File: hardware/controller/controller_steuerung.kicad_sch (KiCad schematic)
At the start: 79 parts, among them J10 FAN, J3 DISPLAY, J4 PANEL, J5 TC top, J6 TC bot, J7 USB-C, J9 UART, Q6 AO3401A, Q7 IRLML6346, Q8 BSS138, SW1 RESET, SW2 BOOT, U10 USBLC6-2SC6, U11 USBLC6-2SC6, U12 USBLC6-2SC6, U3 ESP32-S3-WROOM-1U-N8, U4 USBLC6-2SC6, U5 MAX31856MUD+, U6 MAX31856MUD+

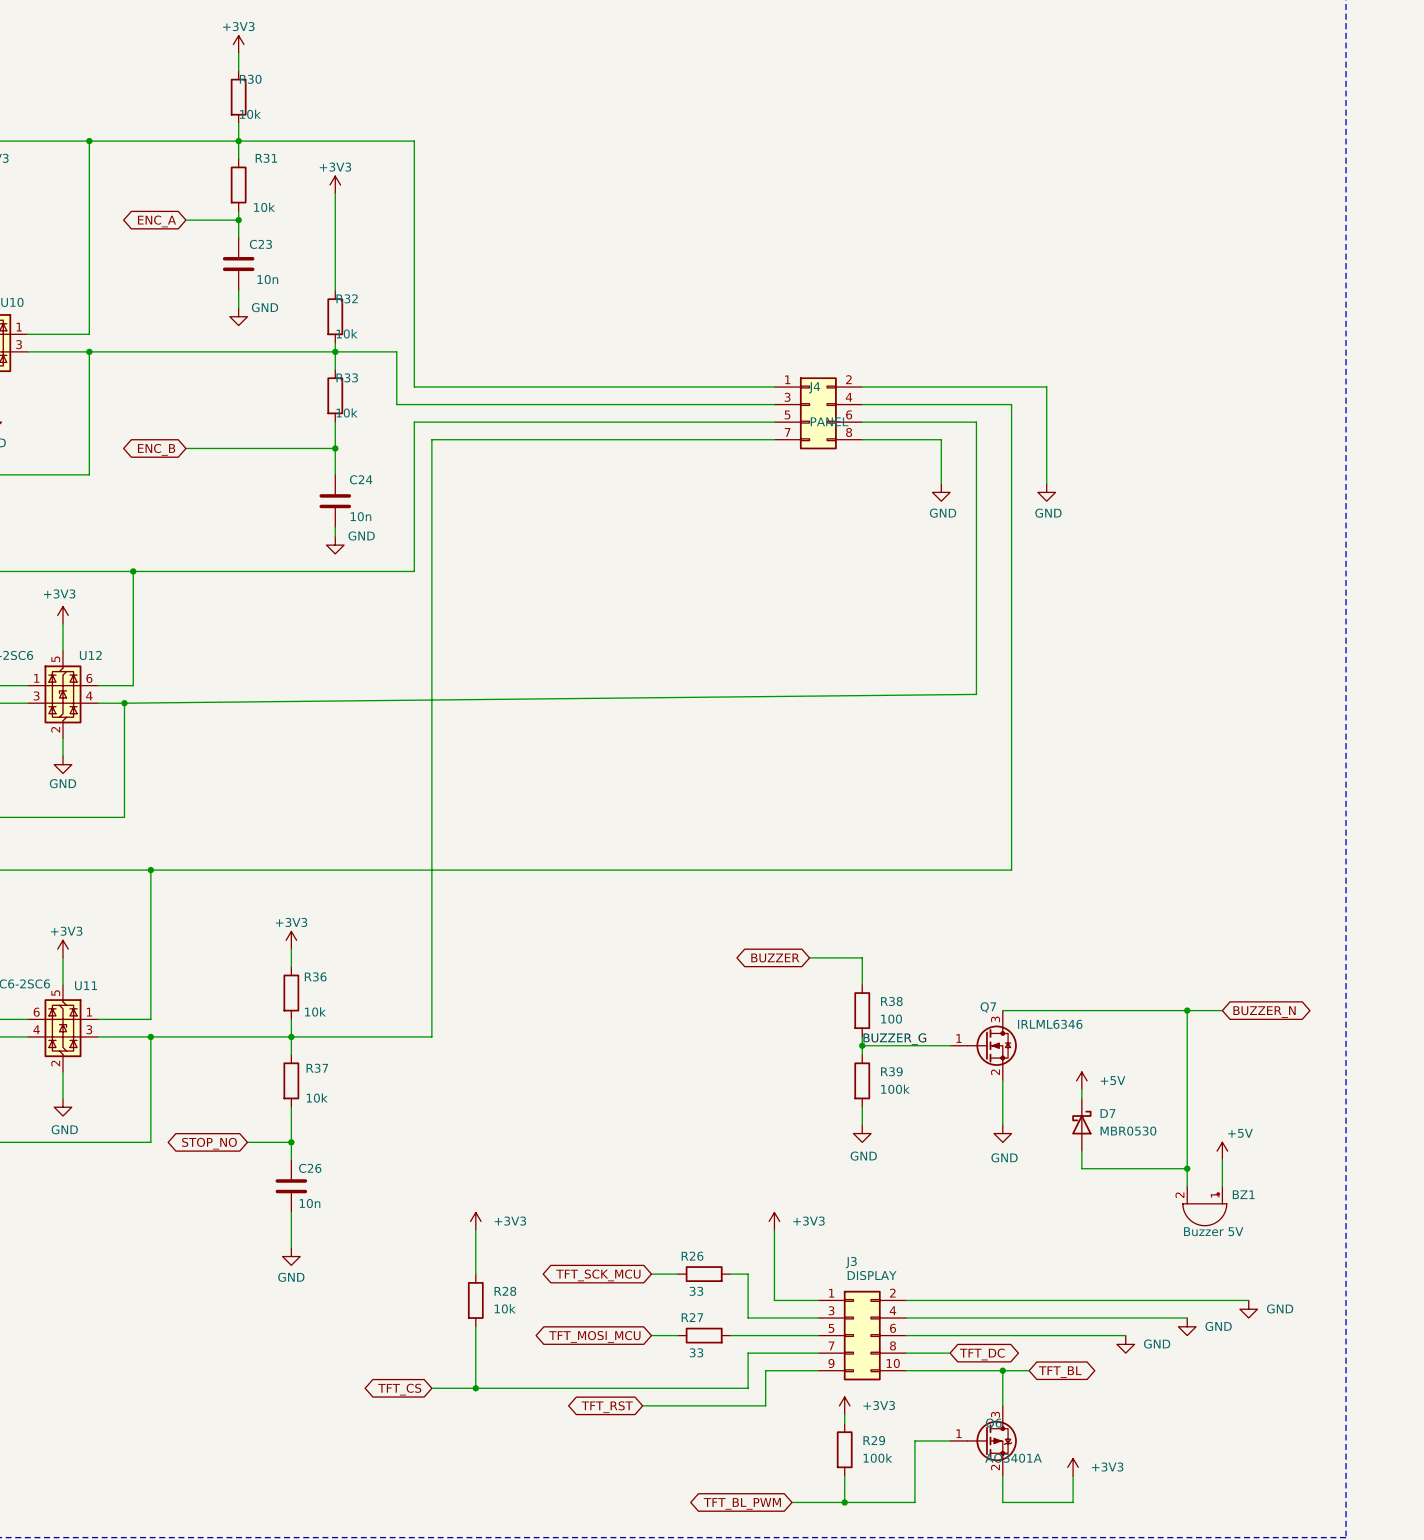
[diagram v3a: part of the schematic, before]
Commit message: feat(hardware): JST XH connectors, re-placement and re-route, open fuse holder (T087, T021)
Connectors (T087, research R9/R10, contracts/connectors.md):
- J3 display JST XH 1x10 (same pin order as the IDC 2x5)
- J4 encoder JST XH 1x5 (A, GND, B, SW, GND), new J11 stop button
  JST XH 1x4 directly on the main board; an unplugged stop connector
  opens the NC loop like a pressed stop button
- encoder carrier: J1 JST XH 1x5, J2 (stop wires) removed
- schematic wire chains of the old connectors replaced by labels,
  connectivity checked pin by pin; ref netlists re-exported

Layout:
- XH connectors at the right edge, RESET/BOOT moved inside
- decoupling capacitors next to their IC pins (LDO 2.6/2.9 mm,
  MAX31856 2.3-3.7 mm, U7/U8/U9 2.2-4.3 mm, ESP32 5.1 mm)
- EMC: flyback diode D7 at the buzzer, 33 ohm SPI resistors at the
  module pins, C1 on the IRM-10-5 output path, thermal vias at the LDO
- re-routed with Freerouting 1.9.0 (2.5.0 compared and rejected),
  GND stitching and isolated GND groups connected
- manual rework by the user: USB D+/D- through the ESD array U4 at the
  connector, tightly coupled, CC2 connected, U4 pin 2 GND connected
- COV1 restored after an accidental delete, dangling stubs removed
- F1: Schurter OGN 0031.8201 open fuse holder instead of the FAB, whose
  carrier is pulled out axially and was blocked by RV1/IRM-10-5;
  L_FUSED re-routed

DRC with schematic parity: 0 errors, 0 unconnected (2 silk edge
warnings from the U1 footprint); check_schematic 0 errors for both
boards; ERC only the documented SDO exclusion.

Co-Authored-By: Claude Opus 5.5 <noreply@anthropic.com>
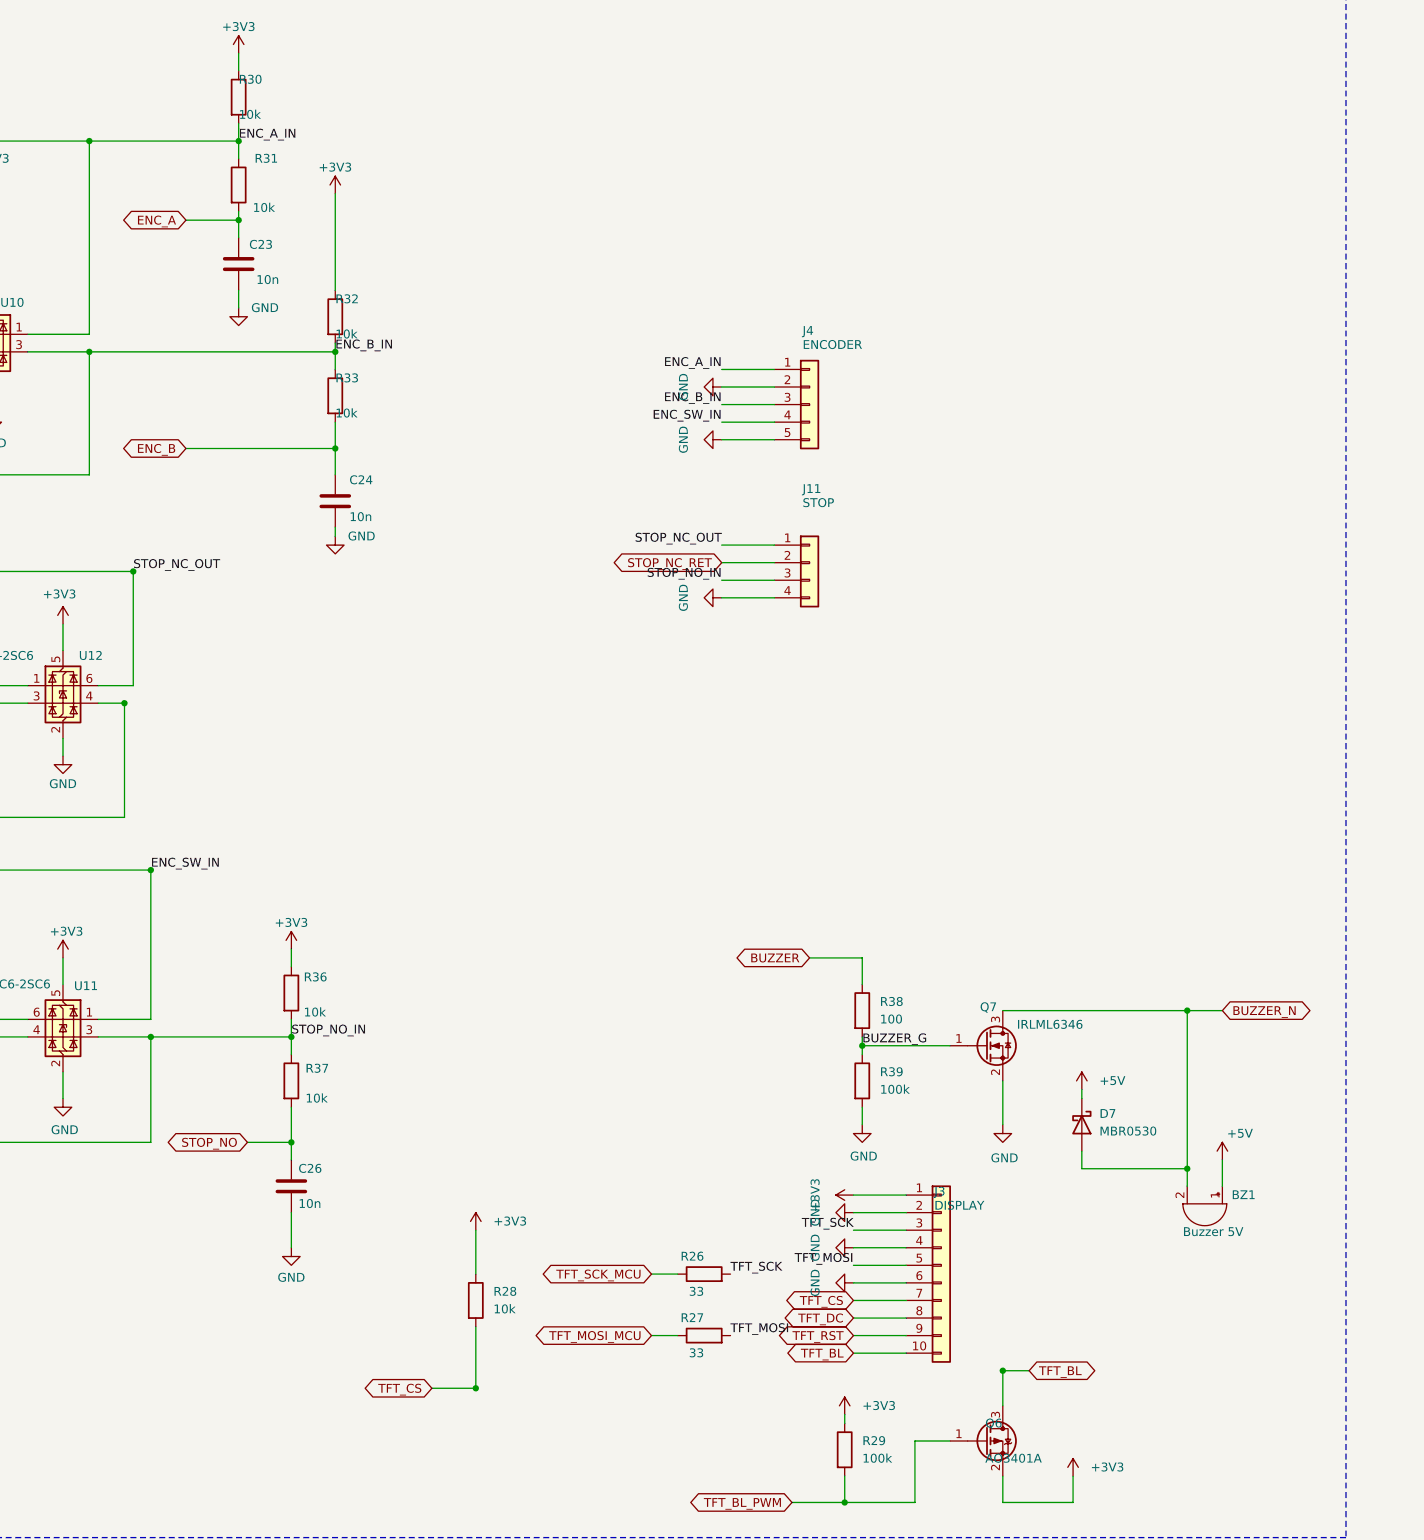
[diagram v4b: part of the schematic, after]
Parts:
- added J11: STOP, Connector_JST:JST_XH_B4B-XH-A_1x04_P2.50mm_Vertical, symbol Connector_Generic:Conn_01x04
- J3: footprint Connector_IDC:IDC-Header_2x05_P2.54mm_Vertical -> Connector_JST:JST_XH_B10B-XH-A_1x10_P2.50mm_Vertical; symbol Connector_Generic:Conn_02x05_Odd_Even -> Connector_Generic:Conn_01x10; MPN Wannenstecker 2x5 RM2.54 -> JST B10B-XH-A
- J4: value PANEL -> ENCODER; footprint Connector_IDC:IDC-Header_2x04_P2.54mm_Vertical -> Connector_JST:JST_XH_B5B-XH-A_1x05_P2.50mm_Vertical; symbol Connector_Generic:Conn_02x04_Odd_Even -> Connector_Generic:Conn_01x05; MPN Wannenstecker 2x4 RM2.54 -> JST B5B-XH-A
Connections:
- net GND: now also J4.5 (Pin_5), J11.4 (Pin_4); no longer J4.8 (Pin_8)
- net STOP_NC_RET: now also J11.2 (Pin_2); no longer J4.6 (Pin_6)
- net ENC_A_IN: now reaches J4.1 (Pin_1), R30.2, R31.1, U10.1 (I/O1), U10.6 (I/O1)
- net TFT_SCK: now reaches J3.3 (Pin_3), R26.2
- net TFT_MOSI: now reaches J3.5 (Pin_5), R27.2
- net STOP_NC_OUT: now reaches R16.2, U12.1 (I/O1), U12.6 (I/O1)
- net STOP_NC_OUT: now also J11.1 (Pin_1); no longer J4.5 (Pin_5)
- net STOP_NO_IN: now reaches R36.2, R37.1, U11.3 (I/O2), U11.4 (I/O2)
- net STOP_NO_IN: now also J11.3 (Pin_3); no longer J4.7 (Pin_7)
- net ENC_SW_IN: now reaches J4.4 (Pin_4), R34.2, R35.1, U11.1 (I/O1), U11.6 (I/O1)
- net ENC_B_IN: now reaches J4.3 (Pin_3), R32.2, R33.1, U10.3 (I/O2), U10.4 (I/O2)
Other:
- moved on the sheet: J3

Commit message: feat(hardware): references renumbered, fixed screw terminals J1/J2, 3D models ESP32/IRM-10
- References re-annotated by sheet position; docs, specs, firmware comment,
  check_schematic.py and DRC rule esp32_thermal_vias (U3 -> U9) updated,
  reference netlist re-exported
- Power symbols no longer excluded from simulation
- J1/J2: Phoenix MKDS 1,5/2-5,08 and MKDS 1/6-3,81 instead of pluggable
  MSTBA/MC; own footprints keep the oval pads (3 mm L-N), generated by
  make_terminal_footprints.py
- 3D models for U9 (Espressif) and U2 (Mean Well) in hardware/lib/3dmodels

Co-Authored-By: Claude Opus 5.5 <noreply@anthropic.com>
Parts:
- renumbered C25 to C10, C9 to C11, C10 to C12, C23 to C13, C6 to C14, C26 to C15, C7 to C16, C24 to C17, C8 to C18, C11 to C19, C31 to C20, C29 to C21, C32 to C22, C17 to C23, C33 to C24, C30 to C25, C12 to C26, C13 to C27, C15 to C28, C16 to C29, C18 to C30, C27 to C31, C14 to C32, C28 to C33, D3 to D4, D7 to D5, D5 to D6, D4 to D7, J5 to J10, J9 to J3, J11 to J5, J3 to J6, J6 to J8, J10 to J9, Q7 to Q6, Q6 to Q7, R16 to R14, R34 to R15, R35 to R16, R1 to R17, R4 to R18, R5 to R19, R2 to R20, R3 to R21, R30 to R22, R31 to R23, R36 to R24, R37 to R25, R32 to R26, R33 to R27, R26 to R29, R27 to R30, R29 to R31, R38 to R32, R39 to R33, R9 to R34, R8 to R35, R6 to R36, R7 to R37, R40 to R38, R41 to R39, R43 to R40, R42 to R41, R11 to R42, R10 to R43, TP12 to TP11, U4 to U10, U6 to U11, U5 to U12, U10 to U6, U12 to U7, U11 to U8, U3 to U9
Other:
- moved on the sheet: C16, C18, C19, C20, C21, C22, C23, C24, C25, C26, C27, C28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
